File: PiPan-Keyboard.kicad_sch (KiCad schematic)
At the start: 137 parts, among them J0 Conn_01x18_MountingPin, SW0 RotaryEncoder_Switch, U1 Pico

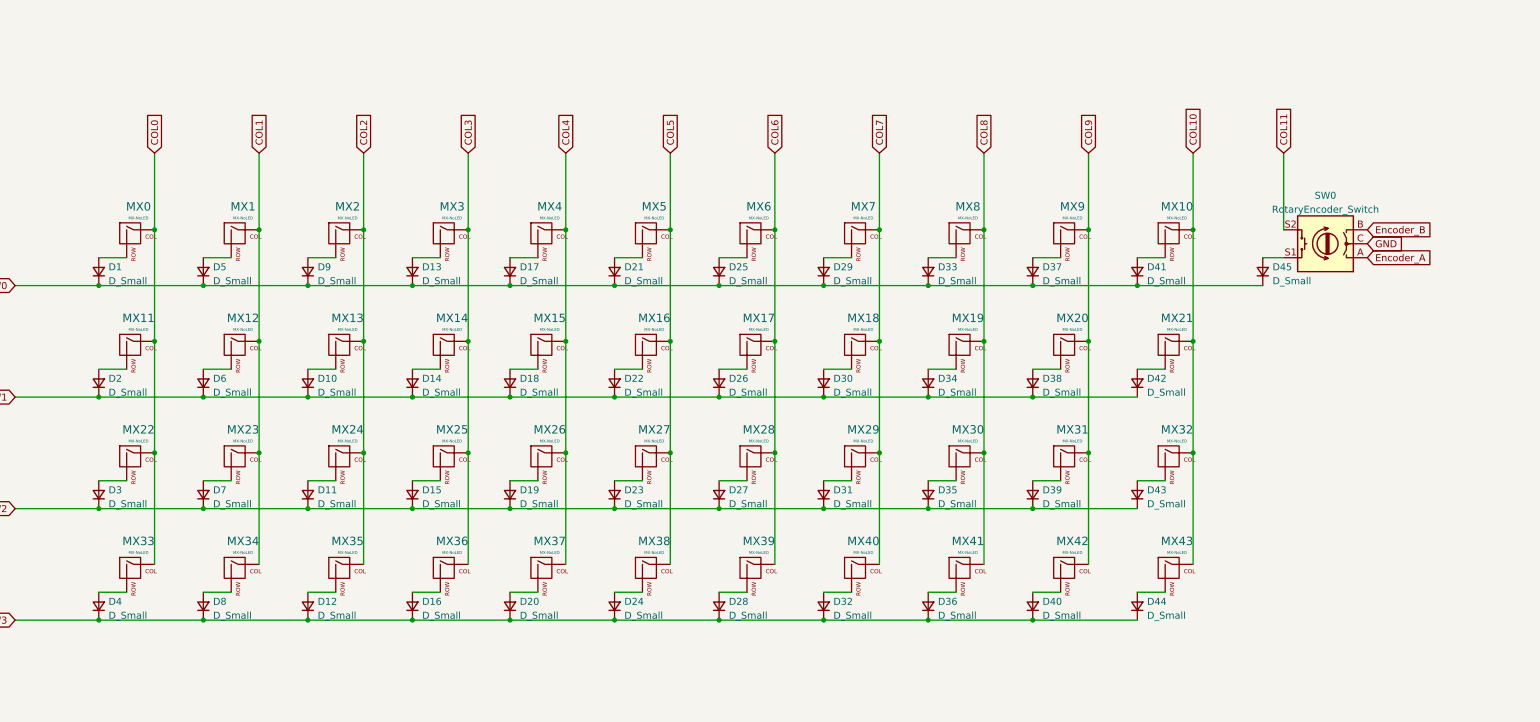
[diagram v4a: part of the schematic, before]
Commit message: corrected switches in schema
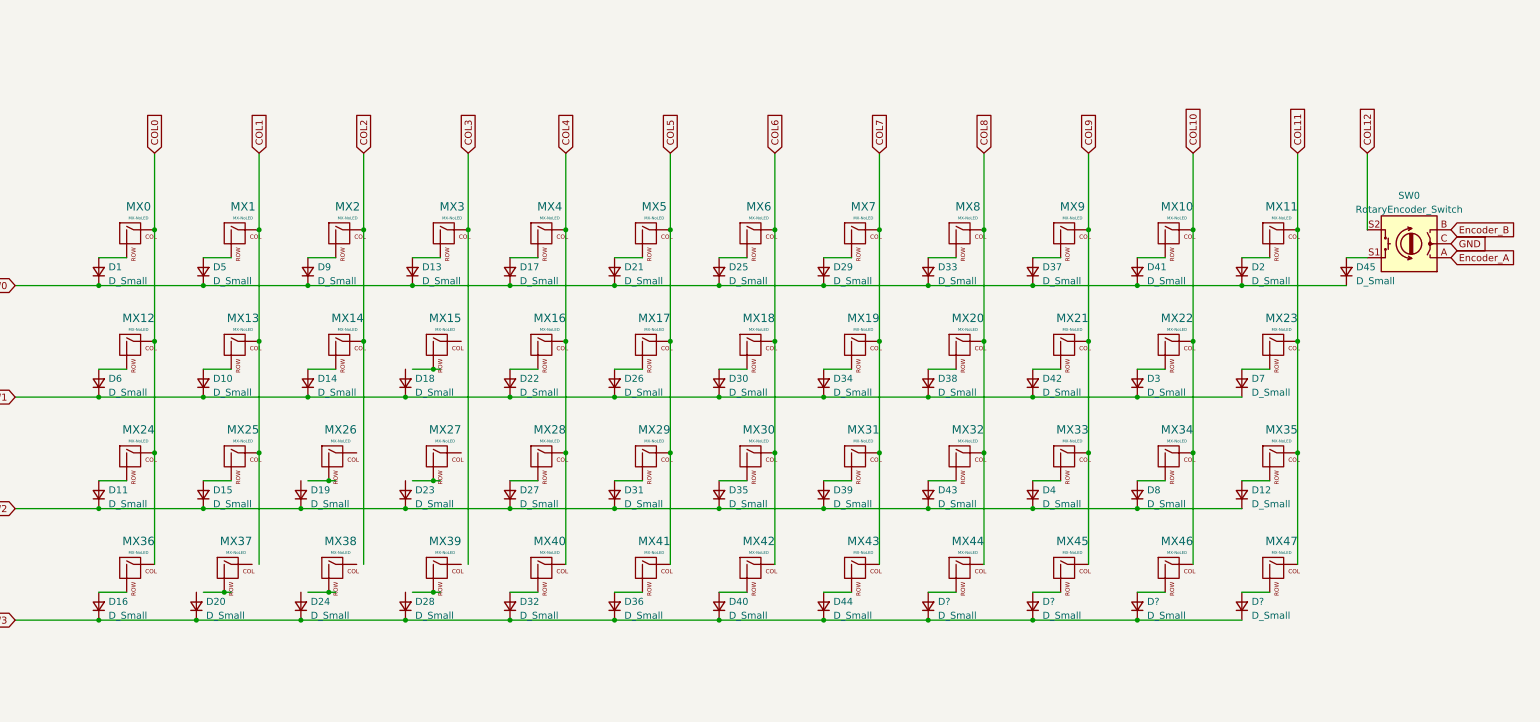
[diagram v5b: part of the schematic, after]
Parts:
- added D? (x4): D_Small, Diode_THT:D_DO-35_SOD27_P10.16mm_Horizontal, symbol Device:D_Small
- added MX44, MX45, MX46, MX47: MX-NoLED, keyswitches:Kailh_socket_MX, symbol MX_Alps_Hybrid:MX-NoLED
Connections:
- net COL0: now also MX12.1 (COL), MX24.1 (COL), MX36.1 (COL); no longer MX11.1 (COL), MX22.1 (COL), MX33.1 (COL)
- net COL1: now also MX13.1 (COL), MX25.1 (COL); no longer MX12.1 (COL), MX23.1 (COL), MX34.1 (COL)
- net COL10: now also MX22.1 (COL), MX34.1 (COL), MX46.1 (COL); no longer MX21.1 (COL), MX32.1 (COL), MX43.1 (COL)
- net COL11: now also MX11.1 (COL), MX23.1 (COL), MX35.1 (COL), MX47.1 (COL); no longer SW0.S2
- net COL2: now also MX14.1 (COL); no longer MX13.1 (COL), MX24.1 (COL), MX35.1 (COL)
- net COL3: no longer MX14.1 (COL), MX25.1 (COL), MX36.1 (COL)
- net COL4: now also MX16.1 (COL), MX28.1 (COL), MX40.1 (COL); no longer MX15.1 (COL), MX26.1 (COL), MX37.1 (COL)
- net COL5: now also MX17.1 (COL), MX29.1 (COL), MX41.1 (COL); no longer MX16.1 (COL), MX27.1 (COL), MX38.1 (COL)
- net COL6: now also MX18.1 (COL), MX30.1 (COL), MX42.1 (COL); no longer MX17.1 (COL), MX28.1 (COL), MX39.1 (COL)
- net COL7: now also MX19.1 (COL), MX31.1 (COL), MX43.1 (COL); no longer MX18.1 (COL), MX29.1 (COL), MX40.1 (COL)
- net COL8: now also MX20.1 (COL), MX32.1 (COL), MX44.1 (COL); no longer MX19.1 (COL), MX30.1 (COL), MX41.1 (COL)
- net COL9: now also MX21.1 (COL), MX33.1 (COL), MX45.1 (COL); no longer MX20.1 (COL), MX31.1 (COL), MX42.1 (COL)
- net ROW0: now also D2.1 (K)
- net ROW1: now also D3.1 (K), D7.1 (K); no longer D2.1 (K)
- net ROW2: now also D12.1 (K), D4.1 (K), D8.1 (K); no longer D3.1 (K), D7.1 (K)
- net ROW3: now also D?.1 (K), D?.1 (K), D?.1 (K), D?.1 (K); no longer D12.1 (K), D4.1 (K), D8.1 (K)
- net at D19.2 (A): no longer MX26.2 (ROW)
- net at D18.2 (A): no longer MX15.2 (ROW)
- net at D28.2 (A): no longer MX39.2 (ROW)
- net at D23.2 (A): no longer MX27.2 (ROW)
- net at MX38.2 (ROW): no longer D24.2 (A)
- net at MX37.2 (ROW): no longer D20.2 (A)
- new net: D?.2 (A), MX46.2 (ROW)
- new net: D?.2 (A), MX47.2 (ROW)
- new net: D?.2 (A), MX44.2 (ROW)
- new net: D?.2 (A), MX45.2 (ROW)
- new net COL12: SW0.S2
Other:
- moved on the sheet: D10, D11, D12, D14, D15, D16, D18, D19, D2, D20, D22, D23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

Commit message: corrected neopixels
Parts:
- added RGB44, RGB45, RGB46, RGB47: SK6812MINI-E, kicad-keyboard-parts:MX_SK6812MINI-E, symbol kicad-keyboard-parts:SK6812MINI-E
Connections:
- net 5V: now also RGB44.1 (VDD), RGB45.1 (VDD), RGB46.1 (VDD), RGB47.1 (VDD); no longer RGB11.1 (VDD), RGB23.1 (VDD), RGB35.1 (VDD)
- net GND: now also RGB44.3 (VSS), RGB45.3 (VSS), RGB46.3 (VSS), RGB47.3 (VSS); no longer RGB11.3 (VSS), RGB23.3 (VSS), RGB35.3 (VSS)
- net RGB1>2: now also RGB11.2 (DOUT), RGB12.4 (DIN); no longer RGB11.4 (DIN)
- net RGB2>3: now also RGB23.2 (DOUT), RGB24.4 (DIN); no longer RGB21.2 (DOUT), RGB22.4 (DIN)
- net RGB3>4: now also RGB35.2 (DOUT), RGB36.4 (DIN); no longer RGB32.2 (DOUT), RGB33.4 (DIN)
- net at RGB43.2 (DOUT): now also RGB44.4 (DIN)
- net at RGB10.2 (DOUT): now also RGB11.4 (DIN)
- new net: RGB46.2 (DOUT), RGB47.4 (DIN)
- new net: RGB32.2 (DOUT), RGB33.4 (DIN)
- new net: RGB45.2 (DOUT), RGB46.4 (DIN)
- new net: RGB44.2 (DOUT), RGB45.4 (DIN)
- new net: RGB21.2 (DOUT), RGB22.4 (DIN)
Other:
- moved on the sheet: RGB11, RGB12, RGB13, RGB14, RGB15, RGB16, RGB17, RGB18, RGB19, RGB20, RGB21, RGB22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

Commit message: updated PCB with added components
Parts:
- gave numbers to parts that had none: 4
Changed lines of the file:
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@@
   (symbol (lib_id "Device:D_Small") (at 379.73 243.84 90) (unit 1)
     (in_bom yes) (on_board yes) (fields_autoplaced)
-    (property "Reference" "D?" (id 0) (at 381.508 243.0053 90)
+    (property "Reference" "D48" (id 0) (at 381.508 243.0053 90)
       (effects (font (size 1.27 1.27)) (justify right))
     )
@@
   (symbol (lib_id "Device:D_Small") (at 398.78 243.84 90) (unit 1)
     (in_bom yes) (on_board yes) (fields_autoplaced)
-    (property "Reference" "D?" (id 0) (at 400.558 243.0053 90)
+    (property "Reference" "D49" (id 0) (at 400.558 243.0053 90)
       (effects (font (size 1.27 1.27)) (justify right))
     )
@@
   (symbol (lib_id "Device:D_Small") (at 341.63 243.84 90) (unit 1)
     (in_bom yes) (on_board yes) (fields_autoplaced)
-    (property "Reference" "D?" (id 0) (at 343.408 243.0053 90)
+    (property "Reference" "D46" (id 0) (at 343.408 243.0053 90)
       (effects (font (size 1.27 1.27)) (justify right))
     )
@@
   (symbol (lib_id "Device:D_Small") (at 360.68 243.84 90) (unit 1)
     (in_bom yes) (on_board yes) (fields_autoplaced)
-    (property "Reference" "D?" (id 0) (at 362.458 243.0053 90)
+    (property "Reference" "D47" (id 0) (at 362.458 243.0053 90)
       (effects (font (size 1.27 1.27)) (justify right))
     )
@@
       (reference "D45") (unit 1) (value "D_Small") (footprint "Diode_THT:D_DO-35_SOD27_P10.16mm_Horizontal")
     )
+    (path "/8387edef-bb57-4ca2-8119-95483e93d1fe"
+      (reference "D46") (unit 1) (value "D_Small") (footprint "Diode_THT:D_DO-35_SOD27_P10.16mm_Horizontal")
+    )
+    (path "/922354d7-a5ee-489a-a941-59b6c9a2e5c0"
+      (reference "D47") (unit 1) (value "D_Small") (footprint "Diode_THT:D_DO-35_SOD27_P10.16mm_Horizontal")
+    )
     (path "/001dfd37-c33c-4a3e-91ca-255ed2e16d8e"
-      (reference "D?") (unit 1) (value "D_Small") (footprint "Diode_THT:D_DO-35_SOD27_P10.16mm_Horizontal")
+      (reference "D48") (unit 1) (value "D_Small") (footprint "Diode_THT:D_DO-35_SOD27_P10.16mm_Horizontal")
     )
     (path "/410cbe9d-5356-4f7b-9692-7e5ced5d5271"
-      (reference "D?") (unit 1) (value "D_Small") (footprint "Diode_THT:D_DO-35_SOD27_P10.16mm_Horizontal")
-    )
-    (path "/8387edef-bb57-4ca2-8119-95483e93d1fe"
-      (reference "D?") (unit 1) (value "D_Small") (footprint "Diode_THT:D_DO-35_SOD27_P10.16mm_Horizontal")
-    )
-    (path "/922354d7-a5ee-489a-a941-59b6c9a2e5c0"
-      (reference "D?") (unit 1) (value "D_Small") (footprint "Diode_THT:D_DO-35_SOD27_P10.16mm_Horizontal")
+      (reference "D49") (unit 1) (value "D_Small") (footprint "Diode_THT:D_DO-35_SOD27_P10.16mm_Horizontal")
     )
     (path "/e6ad8d12-1dbb-4db1-8ba7-443a83a91ca5"

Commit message: fixing diode labels in progress.
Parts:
- renumbered D1 to D0, D2 to D1
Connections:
- net at D1.2 (A): now also MX1.2 (ROW); no longer MX11.2 (ROW)
- net at D5.2 (A): now also MX11.2 (ROW); no longer MX1.2 (ROW)
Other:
- moved on the sheet: D1, D5
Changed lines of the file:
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@@
   (junction (at 294.64 215.9) (diameter 0) (color 0 0 0 0)
   )
+  (junction (at 209.55 185.42) (diameter 0) (color 0 0 0 0)
+  )
   (junction (at 408.94 215.9) (diameter 0) (color 0 0 0 0)
   )
@@
   (junction (at 232.41 241.3) (diameter 0) (color 0 0 0 0)
   )
+  (junction (at 398.78 185.42) (diameter 0) (color 0 0 0 0)
+  )
   (junction (at 322.58 205.74) (diameter 0) (color 0 0 0 0)
   )
@@
   (junction (at 379.73 185.42) (diameter 0) (color 0 0 0 0)
   )
-  (junction (at 398.78 185.42) (diameter 0) (color 0 0 0 0)
-  )
   (junction (at 284.48 205.74) (diameter 0) (color 0 0 0 0)
   )
@@
   (junction (at 275.59 175.26) (diameter 0) (color 0 0 0 0)
   )
-  (junction (at 209.55 185.42) (diameter 0) (color 0 0 0 0)
-  )
   (junction (at 209.55 205.74) (diameter 0) (color 0 0 0 0)
   )
@@
     (stroke (width 0) (type default) (color 0 0 0 0))
   )
-  (wire (pts (xy 209.55 185.42) (xy 228.6 185.42))
-    (stroke (width 0) (type default) (color 0 0 0 0))
-  )
   (wire (pts (xy 364.49 372.11) (xy 374.65 372.11))
     (stroke (width 0) (type default) (color 0 0 0 0))
@@
     (stroke (width 0) (type default) (color 0 0 0 0))
   )
-  (wire (pts (xy 398.78 185.42) (xy 417.83 185.42))
-    (stroke (width 0) (type default) (color 0 0 0 0))
-  )
   (wire (pts (xy 151.13 46.99) (xy 149.86 46.99))
     (stroke (width 0) (type default) (color 0 0 0 0))
@@
     (stroke (width 0) (type default) (color 0 0 0 0))
   )
+  (wire (pts (xy 209.55 185.42) (xy 228.6 185.42))
+    (stroke (width 0) (type default) (color 0 0 0 0))
+  )
+  (wire (pts (xy 398.78 185.42) (xy 417.83 185.42))
+    (stroke (width 0) (type default) (color 0 0 0 0))
+  )
   (wire (pts (xy 149.86 80.01) (xy 151.13 80.01))
     (stroke (width 0) (type default) (color 0 0 0 0))
@@
     (pin "2")
   )
-  (symbol (lib_id "Device:D_Small") (at 398.78 182.88 90) (unit 1)
+  (symbol (lib_id "Device:D_Small") (at 209.55 182.88 90) (unit 1)
     (in_bom yes) (on_board yes) (fields_autoplaced)
-    (property "Reference" "D2" (id 0) (at 400.558 182.0453 90)
+    (property "Reference" "D1" (id 0) (at 211.328 182.0453 90)
       (effects (font (size 1.27 1.27)) (justify right))
     )
-    (property "Value" "D_Small" (id 1) (at 400.558 184.5822 90)
+    (property "Value" "D_Small" (id 1) (at 211.328 184.5822 90)
       (effects (font (size 1.27 1.27)) (justify right))
     )
-    (property "Footprint" "Diode_THT:D_DO-35_SOD27_P10.16mm_Horizontal" (id 2) (at 398.78 182.88 90)
+    (property "Footprint" "Diode_THT:D_DO-35_SOD27_P10.16mm_Horizontal" (id 2) (at 209.55 182.88 90)
       (effects (font (size 1.27 1.27)) hide)
     )
-    (property "Datasheet" "~" (id 3) (at 398.78 182.88 90)
+    (property "Datasheet" "~" (id 3) (at 209.55 182.88 90)
       (effects (font (size 1.27 1.27)) hide)
     )
@@
     (pin "4")
   )
-  (symbol (lib_id "Device:D_Small") (at 209.55 182.88 90) (unit 1)
+  (symbol (lib_id "Device:D_Small") (at 398.78 182.88 90) (unit 1)
     (in_bom yes) (on_board yes) (fields_autoplaced)
-    (property "Reference" "D5" (id 0) (at 211.328 182.0453 90)
+    (property "Reference" "D5" (id 0) (at 400.558 182.0453 90)
       (effects (font (size 1.27 1.27)) (justify right))
     )
-    (property "Value" "D_Small" (id 1) (at 211.328 184.5822 90)
+    (property "Value" "D_Small" (id 1) (at 400.558 184.5822 90)
       (effects (font (size 1.27 1.27)) (justify right))
     )
-    (property "Footprint" "Diode_THT:D_DO-35_SOD27_P10.16mm_Horizontal" (id 2) (at 209.55 182.88 90)
+    (property "Footprint" "Diode_THT:D_DO-35_SOD27_P10.16mm_Horizontal" (id 2) (at 398.78 182.88 90)
       (effects (font (size 1.27 1.27)) hide)
     )
-    (property "Datasheet" "~" (id 3) (at 209.55 182.88 90)
+    (property "Datasheet" "~" (id 3) (at 398.78 182.88 90)
       (effects (font (size 1.27 1.27)) hide)
     )
@@
   (symbol (lib_id "Device:D_Small") (at 190.5 182.88 90) (unit 1)
     (in_bom yes) (on_board yes) (fields_autoplaced)
-    (property "Reference" "D1" (id 0) (at 192.278 182.0453 90)
+    (property "Reference" "D0" (id 0) (at 192.278 182.0453 90)
       (effects (font (size 1.27 1.27)) (justify right))
     )
@@
   (symbol_instances
     (path "/c3545a77-0bf4-4e29-97ba-4e19febf1fb1"
-      (reference "D1") (unit 1) (value "D_Small") (footprint "Diode_THT:D_DO-35_SOD27_P10.16mm_Horizontal")
+      (reference "D0") (unit 1) (value "D_Small") (footprint "Diode_THT:D_DO-35_SOD27_P10.16mm_Horizontal")
     )
     (path "/2995c700-69e7-4dc7-bd18-26e7b043f3cc"
-      (reference "D2") (unit 1) (value "D_Small") (footprint "Diode_THT:D_DO-35_SOD27_P10.16mm_Horizontal")
+      (reference "D1") (unit 1) (value "D_Small") (footprint "Diode_THT:D_DO-35_SOD27_P10.16mm_Horizontal")
     )
     (path "/ca9886cf-bd07-43f5-a054-ad5647199b0a"
